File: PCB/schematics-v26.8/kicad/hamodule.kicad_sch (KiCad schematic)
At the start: 194 parts, among them J1 GND|5V, J10 Tx|Rx, J11 Sda|Scl, J12 3|9, J13 13|12, J14 3.3v|GND|7|15, J15 2604-1104, J16 2604-1104, J17 TestPoint, J19 TestPoint, J2 2604-1102, J3 USB_C_Receptacle_USB2.0, J4 GND|3.3V, J5 Jumper 3.3v, J6 2604-1104, J7 2604-1104, J8 5v|GND|Do, J9 Screen, K1 AQG22205, K2 AQG22205, K3 AQG22205, K4 AQG22205, K5 AQG22205, K6 AQG22205, K7 AQG22205, K8 AQG22205, SW1 USB | PS, SW2 Reset, SW3 Boot, U1 LD1117AV33, U10 SN74LV1T34DBV, U11 ULN2803A, U12 TCAL6416, U14 74AHC1G04, U2 USBLC6-2SC6, U3 ESP32-S3-WROOM-2, U4 LDA210, U5 LDA210, U6 LDA210, U7 LDA210, U8 SHT4x, U9 SN74LVCH8T245

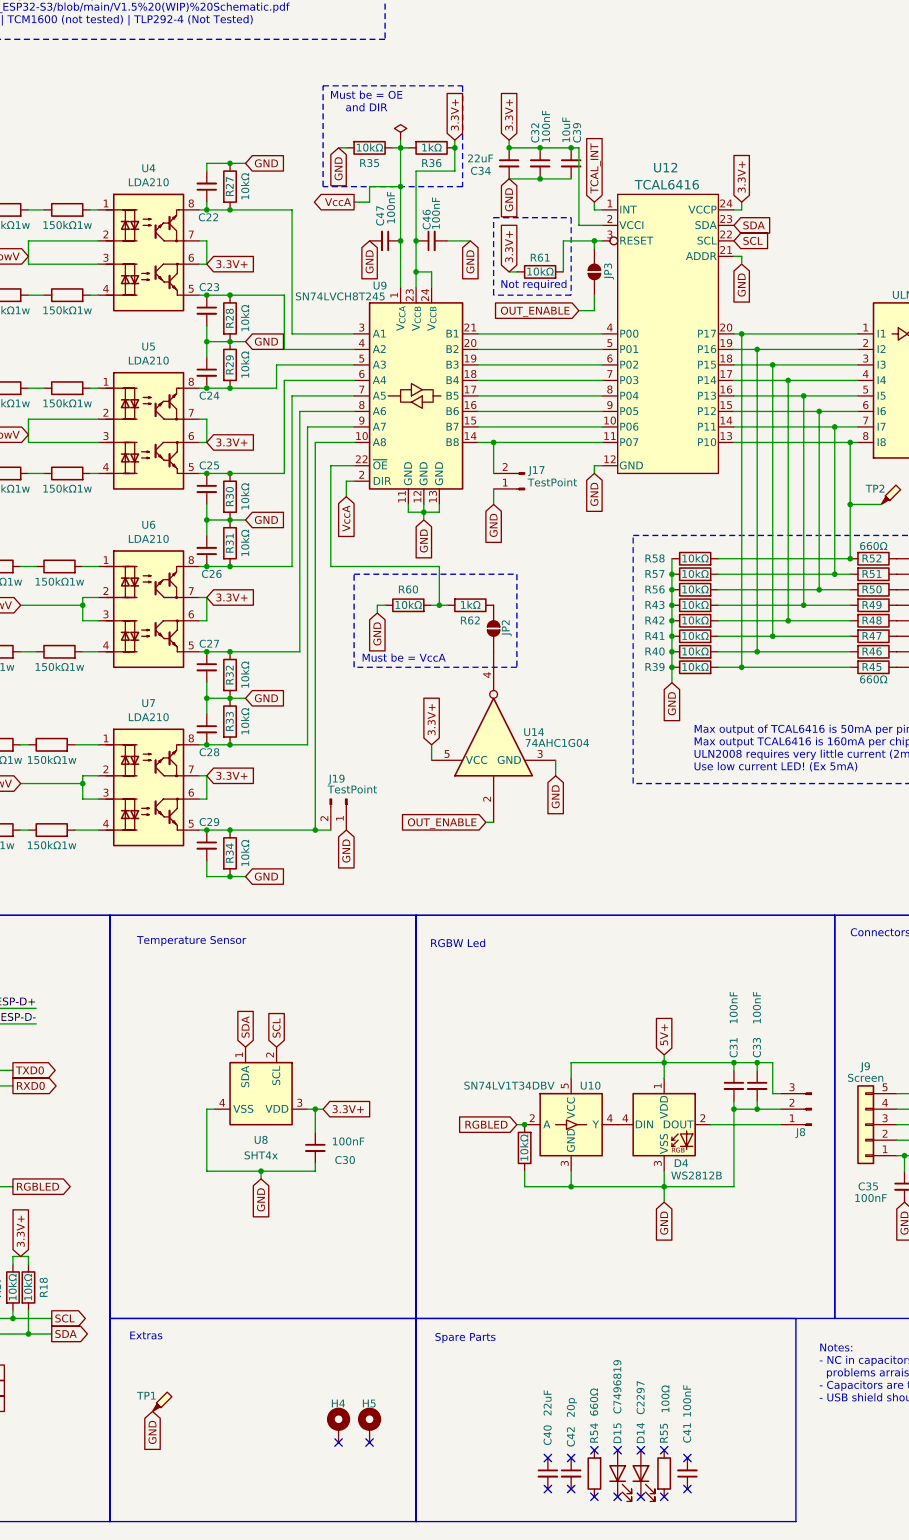
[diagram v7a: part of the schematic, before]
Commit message: Created symbols for every image and logo, in order there are no warnings
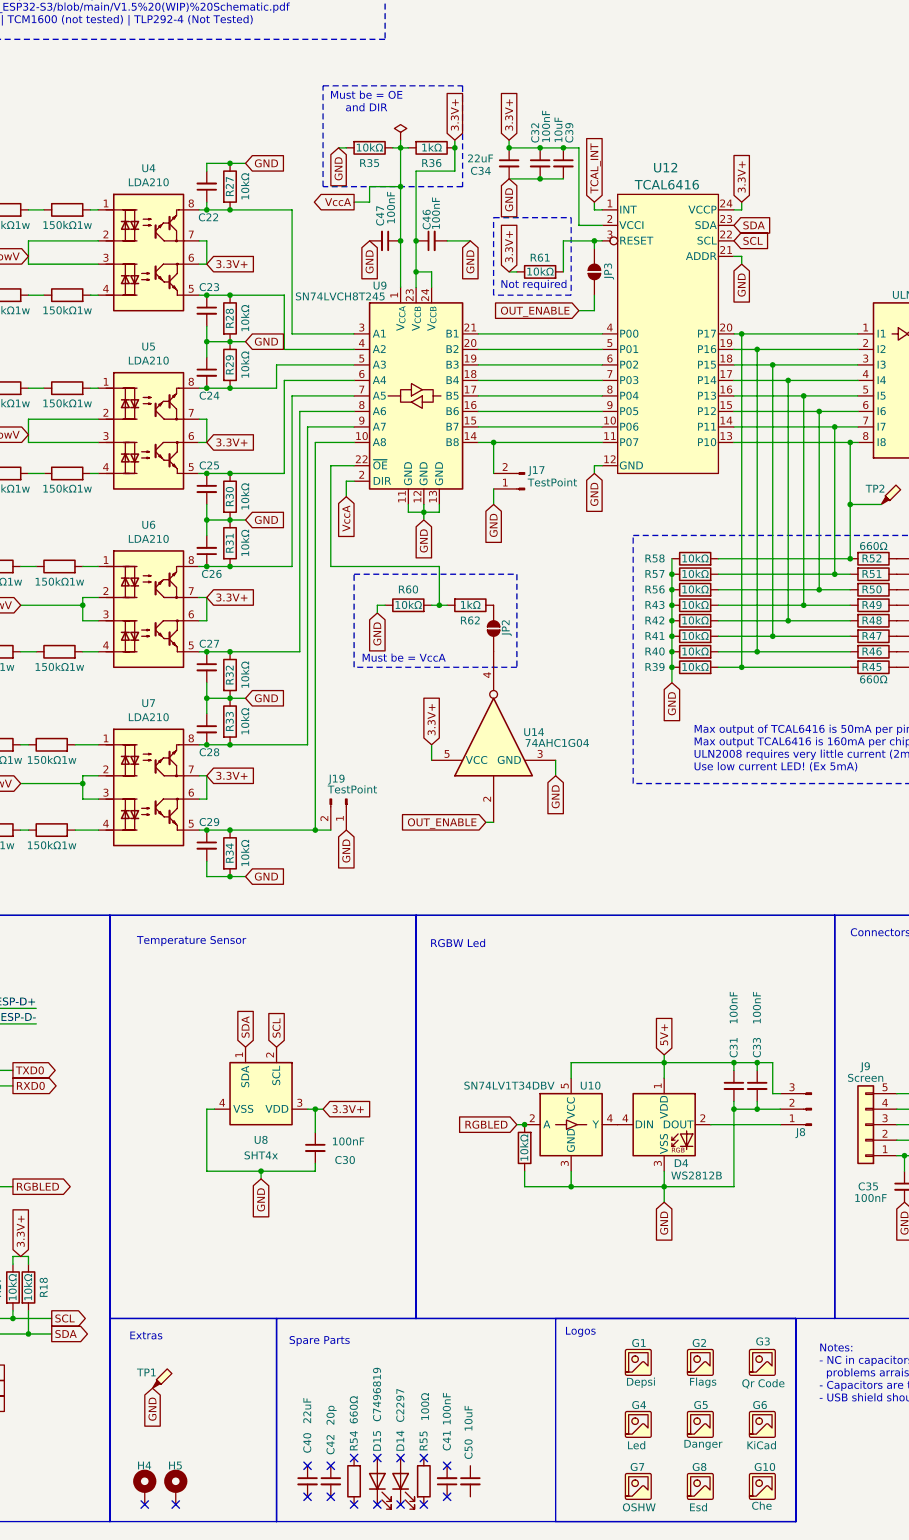
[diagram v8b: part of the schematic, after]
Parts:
- added C50: 10uF, Capacitor_SMD:C_0402_1005Metric, symbol Device:C_Small
- added G1: Depsi, Hamodule_Icons_Footprints:depsi, symbol Hamodule_Icons_Symbols:Depsi
- added G10: Che, Hamodule_Icons_Footprints:che, symbol Hamodule_Icons_Symbols:Che
- added G2: Flags, Hamodule_Icons_Footprints:flags, symbol Hamodule_Icons_Symbols:Flags
- added G3: Qr Code, Hamodule_Icons_Footprints:qr_code, symbol Hamodule_Icons_Symbols:Qr_Code
- added G4: Led, Hamodule_Icons_Footprints:led, symbol Hamodule_Icons_Symbols:Led
- added G5: Danger, Hamodule_Icons_Footprints:danger, symbol Hamodule_Icons_Symbols:Danger
- added G6: KiCad, Symbol:KiCad-Logo2_5mm_SilkScreen, symbol Hamodule_Icons_Symbols:KiCad
- added G7: OSHW, Symbol:OSHW-Logo2_7.3x6mm_SilkScreen, symbol Hamodule_Icons_Symbols:OSHW
- added G8: Esd, Symbol:ESD-Logo_6.6x6mm_SilkScreen, symbol Hamodule_Icons_Symbols:Esd
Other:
- note added: "Logos"
- moved on the sheet: C39, C40, C41, C42, D14, D15, H4, H5, R54, R55, TP1
